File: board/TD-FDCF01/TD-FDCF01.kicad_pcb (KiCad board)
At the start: 2 copper layers, 144 x 144 mm, 64 parts, among them SW1 SW_Push, SW2 SW_Push, SW3 SW_Push

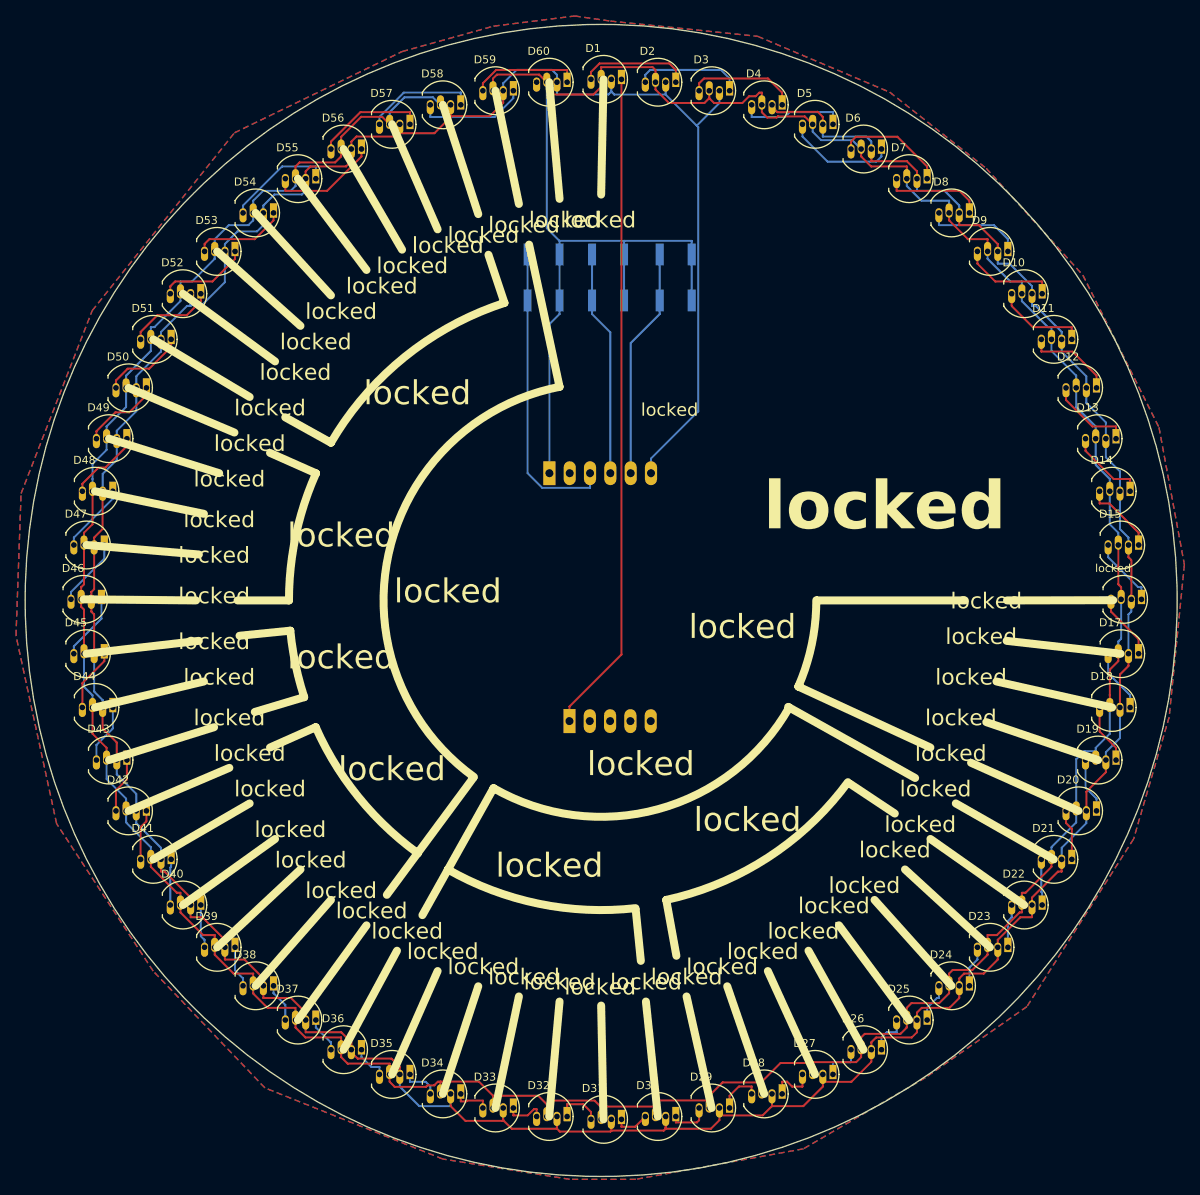
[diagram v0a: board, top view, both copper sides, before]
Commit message: DCF LEDs radially, tweaks to silkscreen
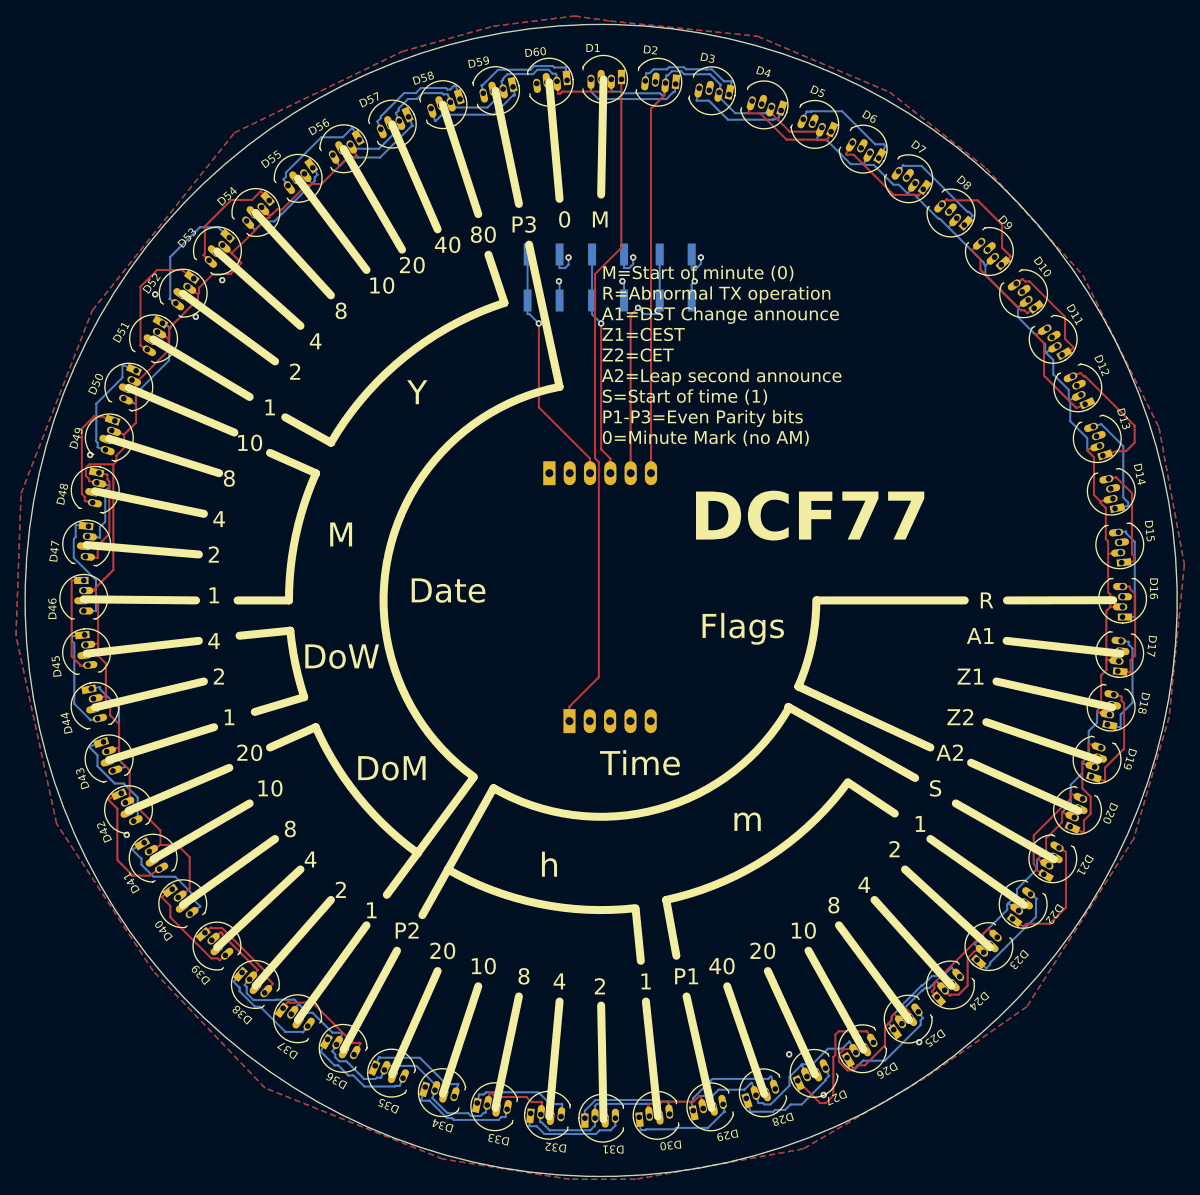
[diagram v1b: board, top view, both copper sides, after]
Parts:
- turned D10 to -54 degrees
- turned D11 to -60 degrees
- turned D12 to -66 degrees
- turned D13 to -72 degrees
- turned D14 to -78 degrees
- turned D15 to -84 degrees
- turned D16 to -90 degrees
- turned D17 to -96 degrees
- turned D18 to -102 degrees
- turned D19 to -108 degrees
- turned D2 to -6 degrees
- turned D20 to -114 degrees
- turned D21 to -120 degrees
- turned D22 to -126 degrees
- turned D23 to -132 degrees
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- renumbered locked to D16, locked to U1
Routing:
- net GND: track 557.9 -> 22.8 mm, vias 0 -> 15
- net +5V: track 526.6 -> 610.8 mm
- net Net-(D26-DOut): track 5.32 -> 19.5 mm
- net Net-(D21-DOut): track 5.75 -> 15.9 mm
- net Net-(D35-DOut): track 4.62 -> 14.5 mm
- net Net-(D41-DOut): track 6.36 -> 16.2 mm
- net Net-(D33-DOut): track 4.65 -> 14.5 mm
- net Net-(D40-DOut): track 5.75 -> 15.6 mm
- net Net-(D34-DOut): track 4.64 -> 14.2 mm
- net Net-(D36-DOut): track 4.52 -> 13.9 mm
- net Net-(D37-DOut): track 4.89 -> 14.1 mm
- net Net-(D25-DOut): track 5.22 -> 14.3 mm
- net /LedA/LEDD_CONT: track 4.44 -> 13.6 mm
- net Net-(D19-DOut): track 6.92 -> 15.7 mm
- net Net-(D29-DOut): track 5.29 -> 14.0 mm
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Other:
- board text added: "0"
- board text added: "1"
- board text added: "10"
- board text added: "2"
- board text added: "20"
- board text added: "4"
- board text added: "40"
- board text added: "8"
- board text added: "80"
- board text added: "A"
- board text added: "A1"
- board text added: "A2"
- board text added: "B"
- board text added: "C"
- board text added: "DCF77"
- board text added: "DCF77 REV.B"
- board text added: "Date"
- board text added: "DoM"
- board text added: "DoW"
- board text added: "Flags"
- board text added: "M"
- board text added: "M=Start of minute (0) R=Abnormal TX operation A1=DST Change announce Z1=CEST Z2=CET A2=Leap second announce S=Start of time (1) P1-P3=Even Parity bits 0=Minute Mark (no AM)"
- board text added: "Mode: Normal Long C: enter/exit test mode A: display mode (1/2/3/4) Long A: enter Time Set mode"
- board text added: "Mode: Time Set A: change value being set B: increment value C: decrement value Long A: exit time set mode"
- board text added: "P1"
- board text added: "P2"
- board text added: "P3"
- board text added: "R"
- board text added: "S"
- board text added: "This is NOT a DCF77 radio controlled clock. This is a clock showing the set time as bits in the DCF77 protocol. NO WEATHER DATA and NO ALERTS PROVIDED Bits 1-14 have fixed values."
- board text added: "Time"
- board text added: "Y"
- board text added: "Z1"
- board text added: "Z2"
- board text added: "h"
- board text added: "m"
- board text removed: "locked"
